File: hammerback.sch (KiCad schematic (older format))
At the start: 45 parts, among them J1 USB_C_Receptacle_USB2.0, P1 USB_C_Plug_USB2.0, U1 MCP73871, U2 TPS61090

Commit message: R0
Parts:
- removed BT1: Battery, KiCad/Connector_JST.pretty:JST_PH_S2B-PH-SM4-TB_1x02-1MP_P2.00mm_Horizontal, symbol Device:Battery
- removed F1: 3 A, KiCad/Capacitor_SMD.pretty:C_1206_3216Metric_Pad1.42x1.75mm_HandSolder, symbol Device:Fuse
- removed TH1: 10k, KiCad/Connector_PinHeader_2.54mm.pretty:PinHeader_1x02_P2.54mm_Vertical, symbol Device:Thermistor
- removed TP1, TP2: TestPoint_Probe, KiCad/TestPoint.pretty:TestPoint_Keystone_5019_Minature, symbol Connector:TestPoint_Probe
- removed TP10, TP5, TP6, TP7, TP8, TP9, TP? (x2): TestPoint, KiCad/TestPoint.pretty:TestPoint_Pad_D1.5mm, symbol Connector:TestPoint
- added H1, H2: MountingHole, KiCad/MountingHole.pretty:MountingHole_3.2mm_M3_ISO14580, symbol Mechanical:MountingHole
- added J2: LiPo, KiCad/Connector_PinHeader_2.54mm.pretty:PinHeader_1x03_P2.54mm_Vertical, symbol Connector_Generic:Conn_01x03
- added TP1, TP2: TestPoint, KiCad/TestPoint.pretty:TestPoint_Pad_D1.5mm, symbol Connector:TestPoint
- renumbered J1 to ee
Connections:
- net GND: now also J2.3 (Pin_3), TP1.1
- net VBUS: now also TP2.1
- net at C1.1, JP1.3 (B), U1.14 (VBAT)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: now also J2.1 (Pin_1)
- net NTC: now reaches R5.2, R6.1
- net NTC: now also J2.2 (Pin_2)
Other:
- moved on the sheet: R6

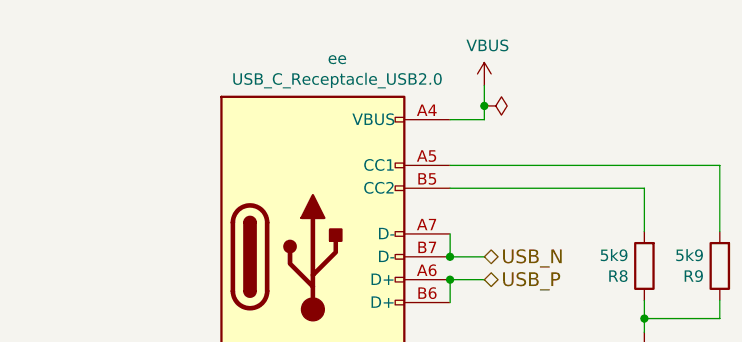
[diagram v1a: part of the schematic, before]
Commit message: fix hole size in pad
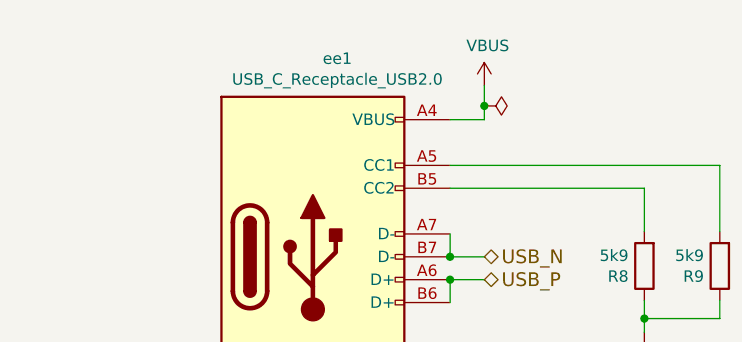
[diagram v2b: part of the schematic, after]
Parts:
- renumbered ee to ee1
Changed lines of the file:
@@
 P 3180 2380
 AR Path="/5E1D22D5/60F26B65" Ref="J?"  Part="1"
-AR Path="/60F26B65" Ref="ee"  Part="1"
+AR Path="/60F26B65" Ref="ee1"  Part="1"
 AR Path="/5E5A3556/60F26B65" Ref="J?"  Part="1"
 AR Path="/5EC66BF7/60F26B65" Ref="J?"  Part="1"
-F 0 "ee" H 3287 3247 50  0000 C CNN
+F 0 "ee1" H 3287 3247 50  0000 C CNN
 F 1 "USB_C_Receptacle_USB2.0" H 3287 3156 50  0000 C CNN
 F 2 "KiCad/Connector_USB.pretty:USB_C_Receptacle_XKB_U262-16XN-4BVC11" H 3330 2380 50  0001 C CNN

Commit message: pcb updates
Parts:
- added JP2: SolderJumper_2_Open, KiCad/Jumper.pretty:SolderJumper-2_P1.3mm_Open_RoundedPad1.0x1.5mm, symbol Jumper:SolderJumper_2_Open
- R14, R15, R8, R9: value 5k9 -> 5k1
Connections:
- net BOOST: now also JP2.1 (A)
- net at C2.1, C3.1, JP1.1 (A)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: now also JP2.2 (B)
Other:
- note added: "Boost is disabled by default here, need to add external switch or pull-up"
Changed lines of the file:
@@
 AR Path="/5EC66BF7/60F26D66" Ref="R?"  Part="1"
 F 0 "R8" H 4699 2466 50  0000 L CNN
-F 1 "5k9" H 4699 2375 50  0000 L CNN
+F 1 "5k1" H 4699 2375 50  0000 L CNN
 F 2 "KiCad/Resistor_SMD.pretty:R_0603_1608Metric" V 4560 2420 50  0001 C CNN
 F 3 "~" H 4630 2420 50  0001 C CNN
@@
 AR Path="/5EC66BF7/60F26D70" Ref="R?"  Part="1"
 F 0 "R9" H 5029 2466 50  0000 L CNN
-F 1 "5k9" H 5029 2375 50  0000 L CNN
+F 1 "5k1" H 5029 2375 50  0000 L CNN
 F 2 "KiCad/Resistor_SMD.pretty:R_0603_1608Metric" V 4890 2420 50  0001 C CNN
 F 3 "~" H 4960 2420 50  0001 C CNN
@@
 Connection ~ 9520 6430
 Wire Wire Line
-	9520 6430 9520 6130
+	9520 6430 9520 6330
 Wire Wire Line
 	9520 6130 10430 6130
@@
 AR Path="/5EC66BF7/60F3328D" Ref="R?"  Part="1"
 F 0 "R15" H 11779 2516 50  0000 L CNN
-F 1 "5k9" H 11779 2425 50  0000 L CNN
+F 1 "5k1" H 11779 2425 50  0000 L CNN
 F 2 "KiCad/Resistor_SMD.pretty:R_0603_1608Metric" V 11640 2470 50  0001 C CNN
 F 3 "~" H 11710 2470 50  0001 C CNN
@@
 AR Path="/5EC66BF7/60F33294" Ref="R?"  Part="1"
 F 0 "R14" H 11449 2516 50  0000 L CNN
-F 1 "5k9" H 11449 2425 50  0000 L CNN
+F 1 "5k1" H 11449 2425 50  0000 L CNN
 F 2 "KiCad/Resistor_SMD.pretty:R_0603_1608Metric" V 11310 2470 50  0001 C CNN
 F 3 "~" H 11380 2470 50  0001 C CNN
@@
 $EndComp
 Connection ~ 2880 3390
+Text Notes 9850 7890 0    50   ~ 0
+Boost is disabled by default here, need to add external switch or pull-up
+Text HLabel 8730 6330 0    50   Input ~ 0
+BOOST
+Wire Wire Line
+	8730 6330 8830 6330
+$Comp
+L Jumper:SolderJumper_2_Open JP2
+U 1 1 61383F10
+P 8980 6330
+F 0 "JP2" H 8980 6535 50  0000 C CNN
+F 1 "SolderJumper_2_Open" H 8980 6444 50  0000 C CNN
+F 2 "KiCad/Jumper.pretty:SolderJumper-2_P1.3mm_Open_RoundedPad1.0x1.5mm" H 8980 6330 50  0001 C CNN
+F 3 "~" H 8980 6330 50  0001 C CNN
+	1    8980 6330
+	1    0    0    -1
+$EndComp
+Wire Wire Line
+	9130 6330 9520 6330
+Connection ~ 9520 6330
+Wire Wire Line
+	9520 6330 9520 6130
 $EndSCHEMATC
